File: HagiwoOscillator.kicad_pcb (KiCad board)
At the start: 2 copper layers, 48 parts, among them J1 Conn_02x05_Odd_Even, J2 out, J3 Conn_01x03, J4 1v/oct, J5 in1, J6 in1, U1 TL072, U2 L7805

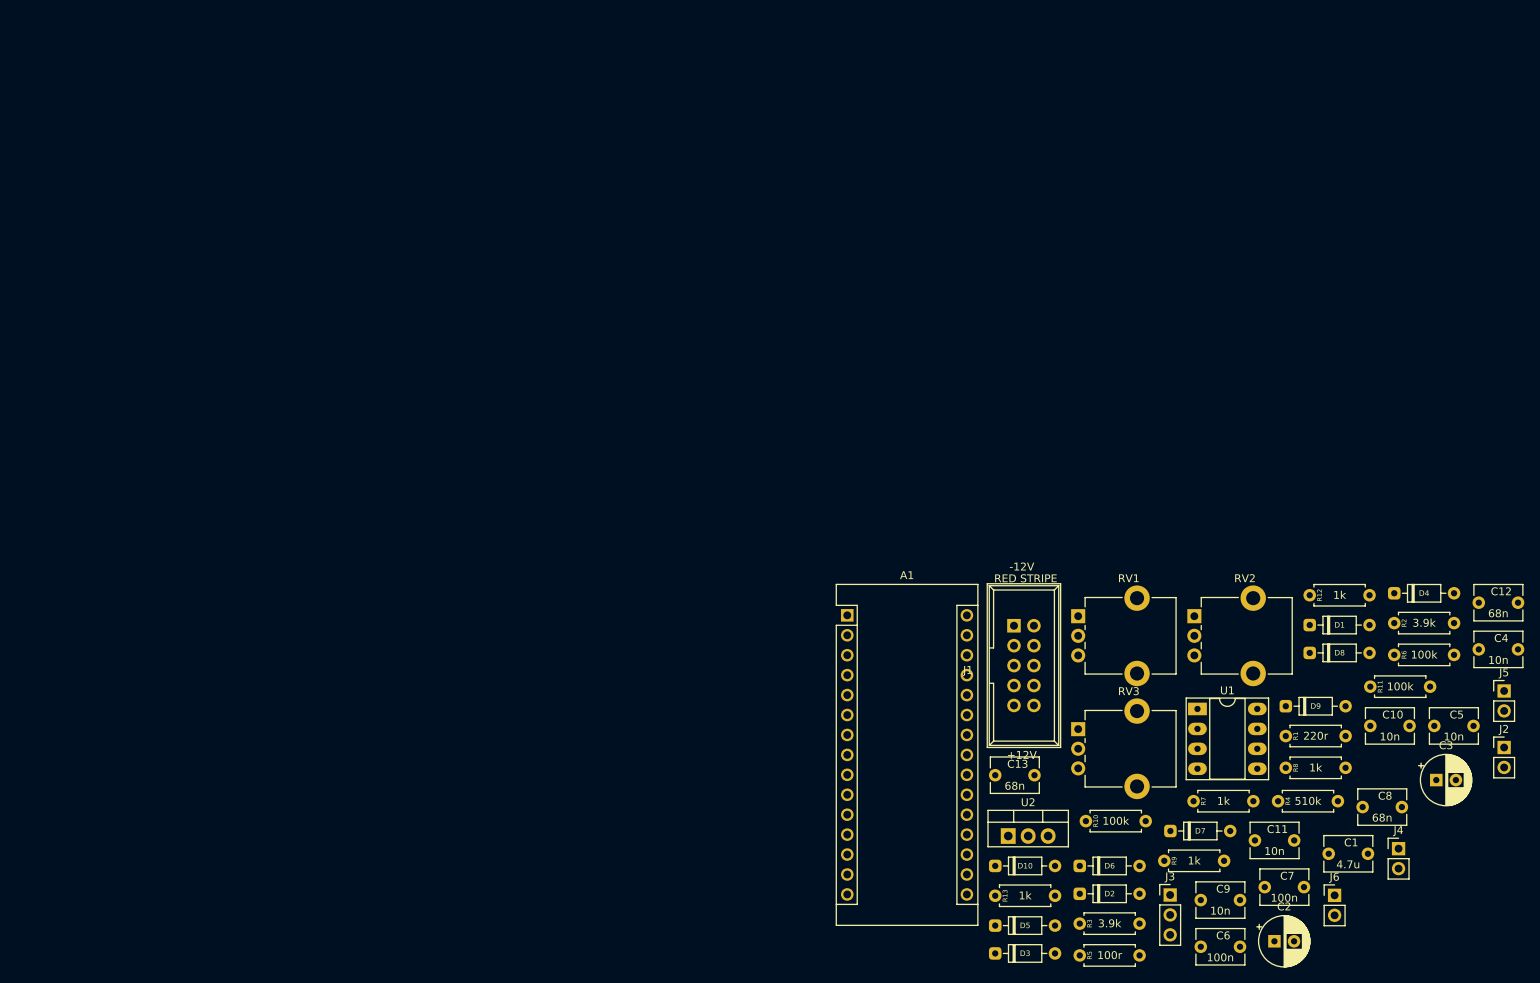
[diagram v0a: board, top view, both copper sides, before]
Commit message: place duino and pots
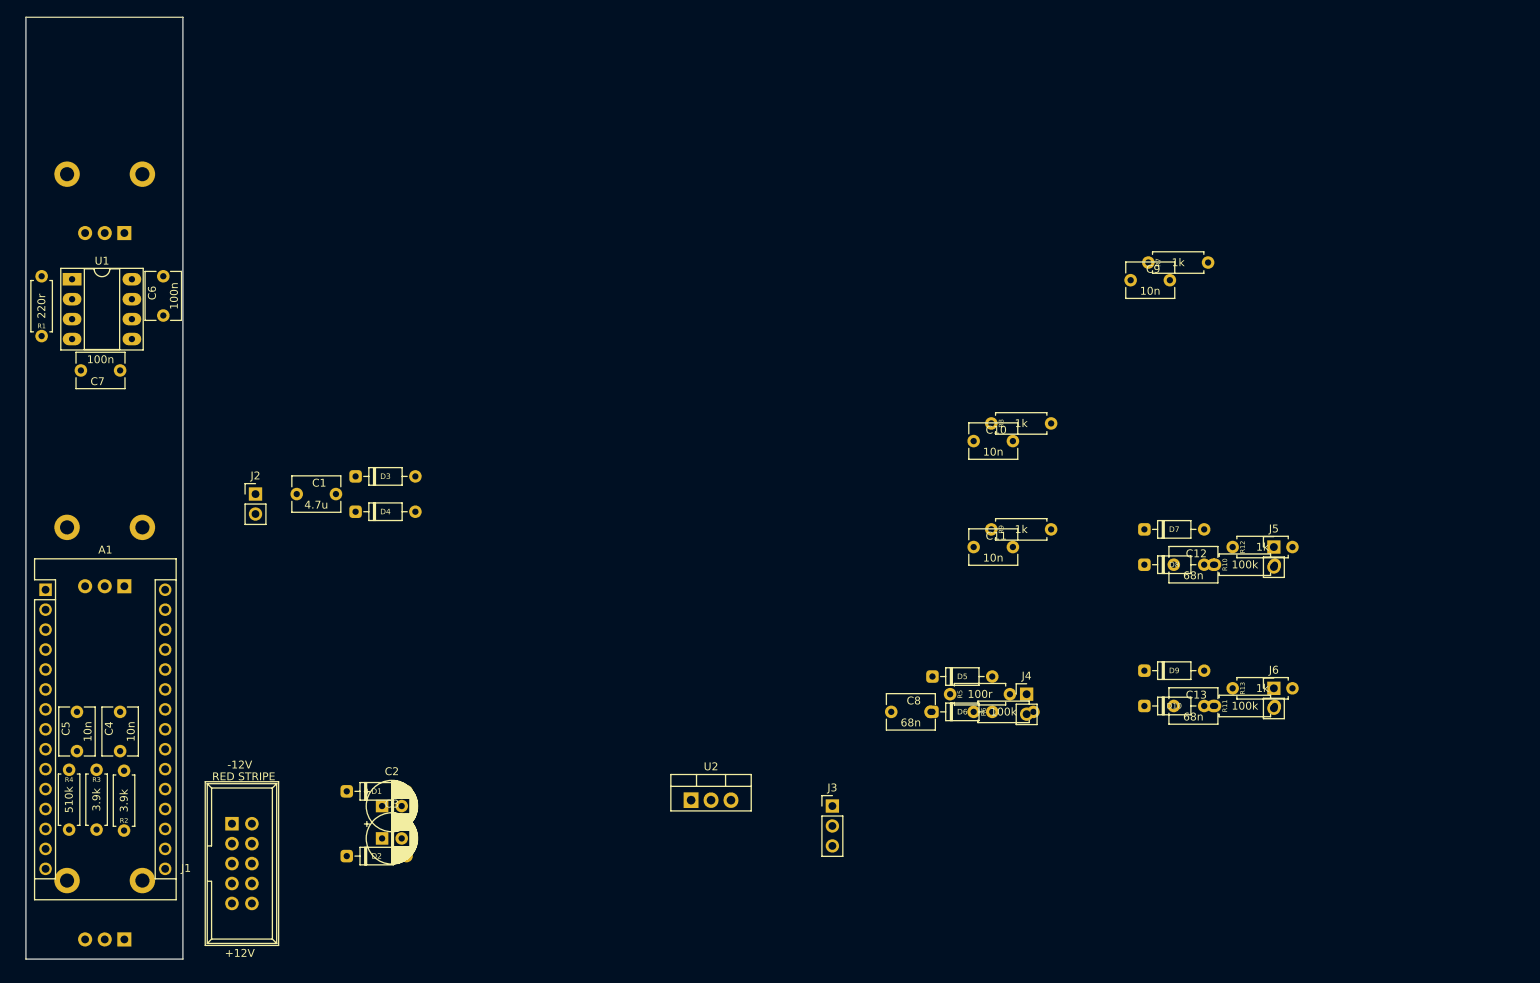
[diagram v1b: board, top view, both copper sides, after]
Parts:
- RV1, RV2, RV3: moved to B.Cu
- moved C4 173.6 mm to (12.0, 93.5), turned to 90 degrees
- moved C5 173.0 mm to (6.50, 93.5), turned to 90 degrees
- moved R1 166.5 mm to (2.00, 40.6), turned to 90 degrees
- moved R2 164.0 mm to (12.5, 103.6), turned to 90 degrees
- moved J2 162.3 mm to (29.2, 60.8)
- moved C7 160.0 mm to (12.0, 45.0), turned to 180 degrees
- moved C6 154.7 mm to (17.5, 38.0), turned to 90 degrees
- moved R4 154.1 mm to (5.50, 95.9), turned to 270 degrees
- moved U1 153.5 mm to (5.88, 33.4)
- moved RV2 147.0 mm to (10.0, 65.0), turned to 90 degrees
- moved RV1 144.1 mm to (10.0, 20.0), turned to 90 degrees
- moved C1 139.2 mm to (34.5, 60.8)
- moved C3 134.5 mm to (45.4, 104.6)
- moved D4 132.7 mm to (42.0, 63.0)
- moved RV3 132.6 mm to (10.0, 110.0), turned to 90 degrees
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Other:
- board outline added: 20 x 120 mm

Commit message: update pcb from schem
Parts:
- J1: footprint Sonosus:Power_Header -> Connector_PinHeader_2.54mm:PinHeader_2x05_P2.54mm_Vertical
- moved J1 100.9 mm to (15.0, 2.46), turned to 270 degrees
- moved C3 99.9 mm to (12.0, 10.5)
- moved C2 99.7 mm to (2.50, 10.5)
- moved D2 91.1 mm to (2.00, 24.5), turned to 90 degrees
- moved D1 84.9 mm to (18.0, 16.9), turned to 270 degrees
- moved D4 37.2 mm to (5.88, 54.0)
- moved D3 36.2 mm to (5.88, 56.5)
- moved C1 29.5 mm to (7.00, 50.0)
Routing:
- added copper zone on B.Cu, net GND
- added copper zone on F.Cu, net GND

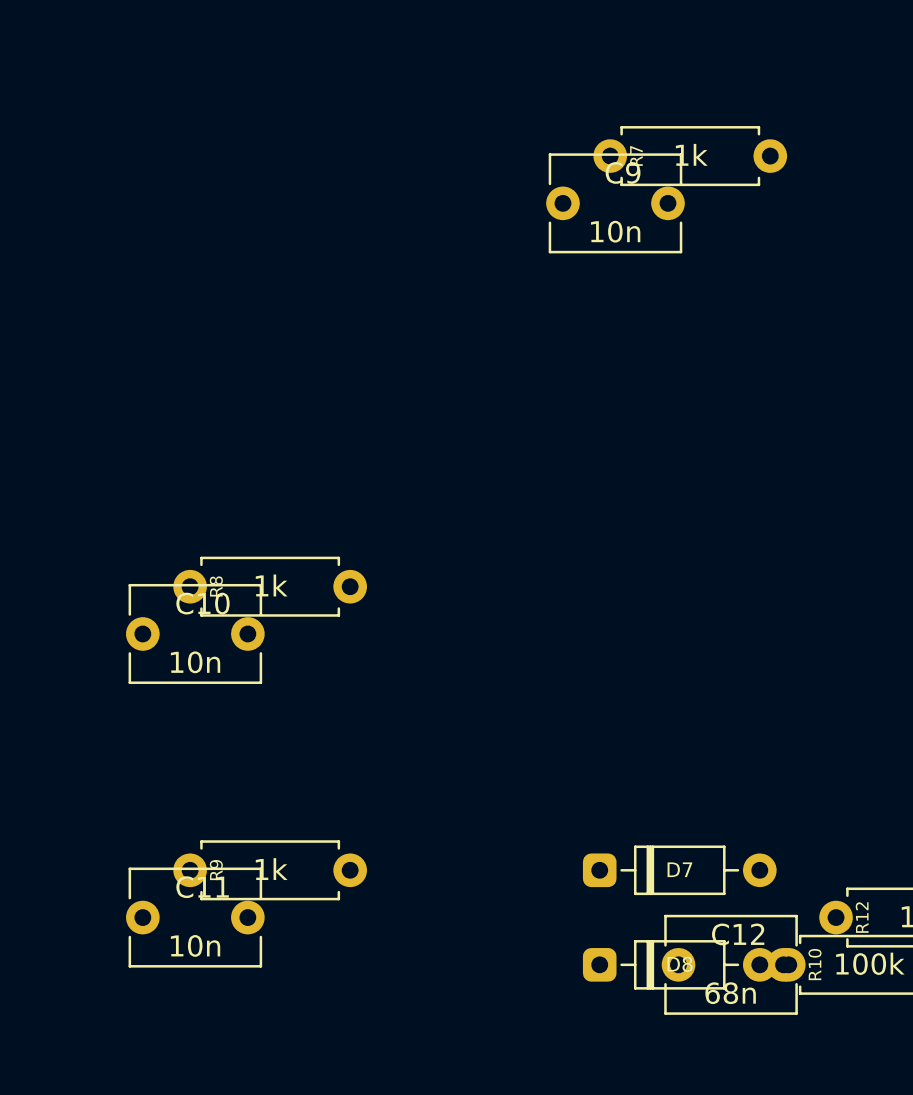
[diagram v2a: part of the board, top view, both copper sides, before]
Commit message: update pcb from schem
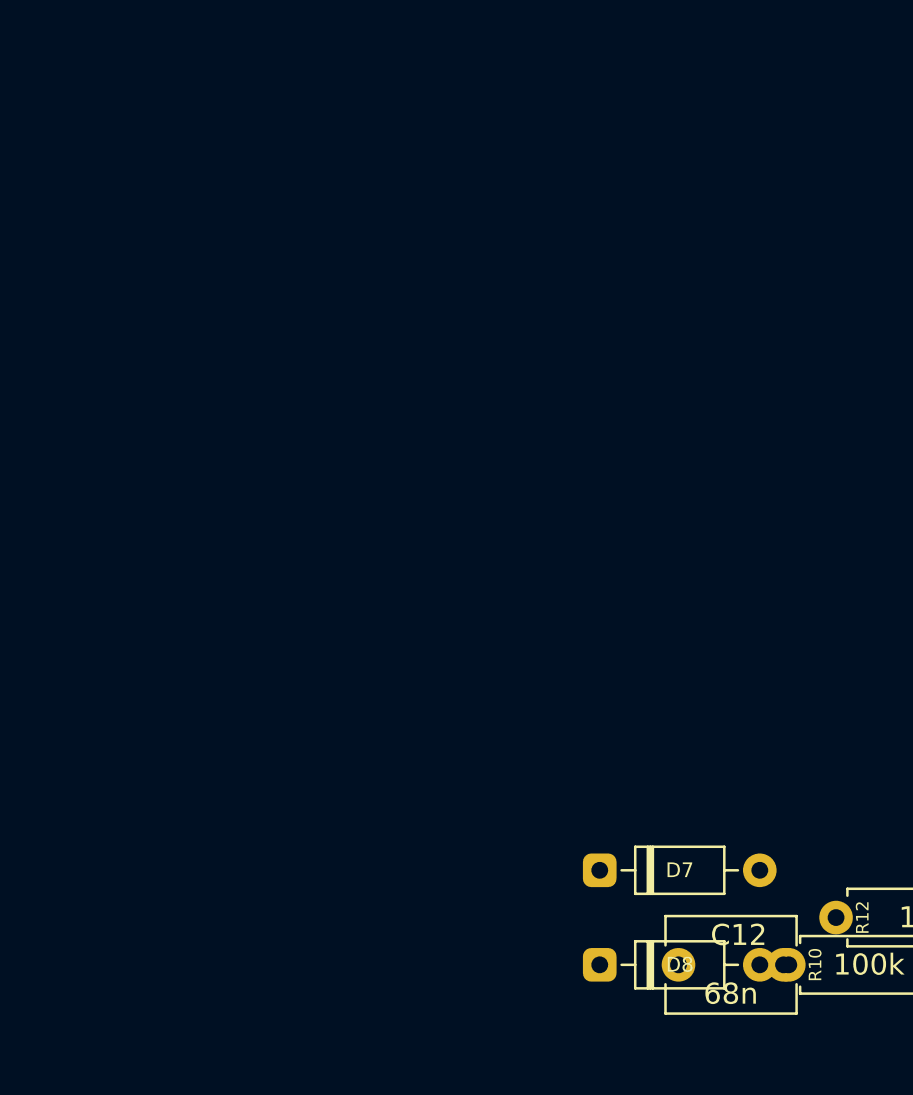
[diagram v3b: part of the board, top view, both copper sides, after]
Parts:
- removed C10, C11, C9: 10n, Sonosus:Capacitor_NonPolarized
- removed R7, R8, R9: 1k, Sonosus:Resistor
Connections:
- RV1 pad 2: Net-(R7-Pad2) -> Net-(A1-Pad19)
- RV2 pad 2: Net-(R8-Pad2) -> Net-(A1-Pad20)
- RV3 pad 2: Net-(R9-Pad2) -> Net-(A1-Pad22)

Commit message: place all components
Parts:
- R11, R12, R13, R2, R3, R4: footprint Sonosus:Resistor -> Resistor_THT:R_Axial_DIN0207_L6.3mm_D2.5mm_P2.54mm_Vertical
- moved J6 156.4 mm to (5.50, 115.5)
- moved R12 150.6 mm to (7.00, 101.5), turned to 270 degrees
- moved J5 149.4 mm to (17.5, 115.5)
- moved R13 144.4 mm to (10.2, 101.5), turned to 270 degrees
- moved C13 138.8 mm to (10.0, 114.2), turned to 90 degrees
- moved R10 138.8 mm to (13.1, 80.5), turned to 180 degrees
- moved R11 138.7 mm to (13.5, 101.5), turned to 270 degrees
- moved D7 138.2 mm to (5.50, 83.5)
- moved D8 138.0 mm to (5.50, 86.2)
- moved C12 133.5 mm to (12.8, 68.8), turned to 180 degrees
- moved D10 129.9 mm to (13.0, 77.5), turned to 180 degrees
- moved D9 129.8 mm to (13.0, 74.8), turned to 180 degrees
- moved J4 129.0 mm to (1.82, 115.5)
- moved R6 117.9 mm to (6.88, 58.0)
- moved D6 117.0 mm to (1.50, 62.0), turned to 90 degrees
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
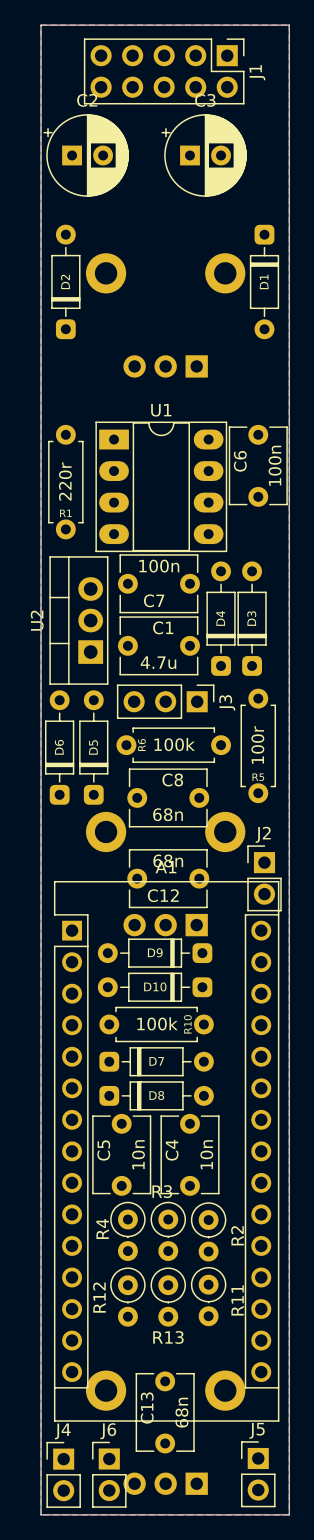
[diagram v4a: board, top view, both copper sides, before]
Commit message: routed, still many pcb errors
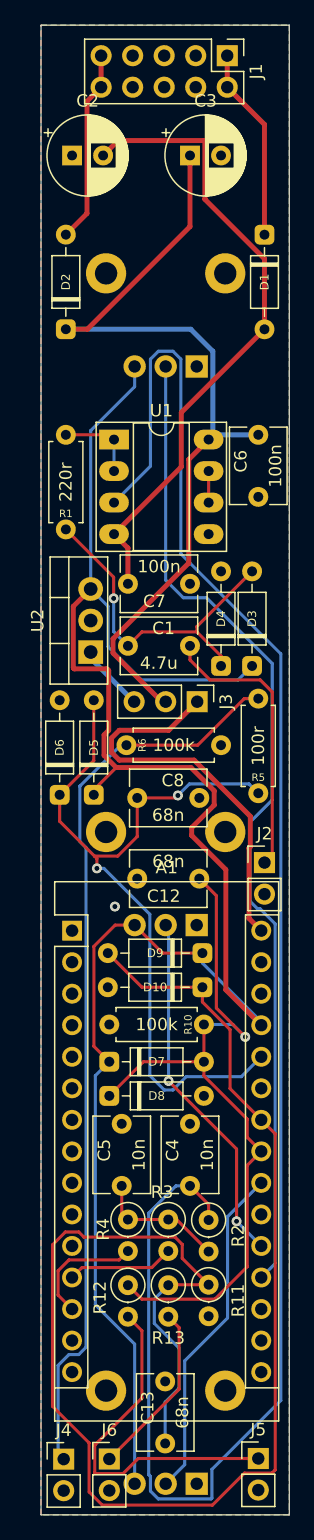
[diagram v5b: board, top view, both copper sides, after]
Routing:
- net +5V: track 0.00 -> 153.4 mm
- net Net-(C4-Pad1): track 0.00 -> 148.4 mm
- net Net-(A1-Pad24): track 0.00 -> 121.0 mm
- net Net-(A1-Pad19): track 0.00 -> 80.2 mm
- net Net-(J4-Pad1): track 0.00 -> 73.3 mm
- net +12V: track 0.00 -> 69.4 mm
- net Net-(A1-Pad26): track 0.00 -> 63.0 mm, vias 0 -> 2
- net Net-(A1-Pad23): track 0.00 -> 59.8 mm, vias 0 -> 1
- net -12V: track 0.00 -> 51.8 mm
- net VIN: track 0.00 -> 32.2 mm
- net Net-(A1-Pad20): track 0.00 -> 29.0 mm, vias 0 -> 2
- net Net-(J5-Pad1): track 0.00 -> 28.3 mm
- net Net-(C1-Pad1): track 0.00 -> 27.7 mm, vias 0 -> 1
- net Net-(A1-Pad22): track 0.00 -> 27.4 mm
- net Net-(C1-Pad2): track 0.00 -> 22.8 mm
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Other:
- copper layers 2 -> 4

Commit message: fix 3dm
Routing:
- net GND: track 0.00 -> 37.7 mm, vias 1 -> 5
- net +12V: track 69.4 -> 74.2 mm
- net (no net): track 0.00 -> 1.70 mm, vias 0 -> 1
- net Net-(J6-Pad1): track 14.2 -> 13.4 mm
- net -12V: track 51.8 -> 52.4 mm
